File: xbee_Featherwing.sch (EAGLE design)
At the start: 17 parts

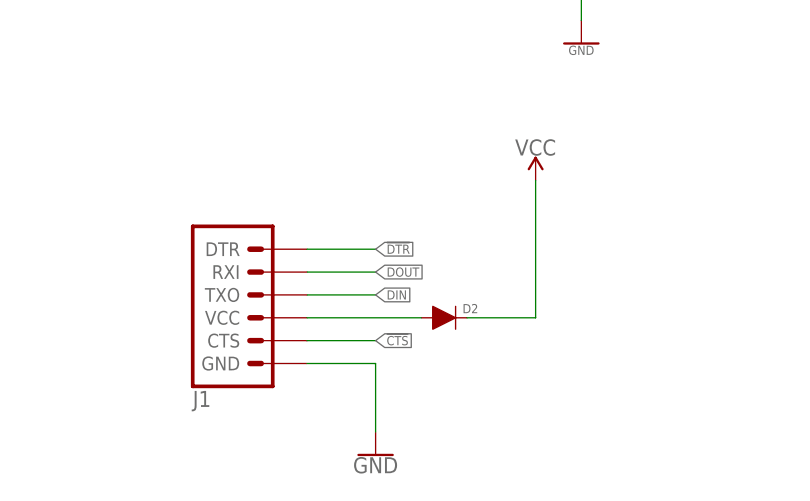
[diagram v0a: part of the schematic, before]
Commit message: Changing footprint
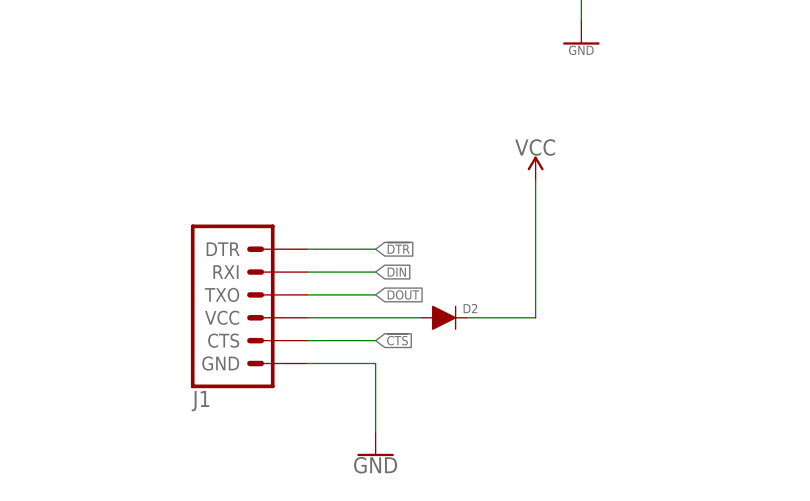
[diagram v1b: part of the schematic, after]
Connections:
- net DIN: now also J1.RXI; no longer J1.TXO
- net DOUT: now also J1.TXO; no longer J1.RXI
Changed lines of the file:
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@@
 <?xml version="1.0" encoding="utf-8"?>
 <!DOCTYPE eagle SYSTEM "eagle.dtd">
-<eagle version="9.5.0">
+<eagle version="9.4.1">
 <drawing>
 <settings>
@@
 </segment>
 <segment>
+<pinref part="MS1" gate="G$1" pin="GPIORX"/>
+<wire x1="55.88" y1="93.98" x2="50.8" y2="93.98" width="0.1524" layer="91"/>
+<label x="50.8" y="93.98" size="1.016" layer="95" font="vector" ratio="20" rot="R180" xref="yes"/>
+</segment>
+<segment>
+<pinref part="J1" gate="G$1" pin="TXO"/>
+<wire x1="185.42" y1="60.96" x2="193.04" y2="60.96" width="0.1524" layer="91"/>
+<label x="193.04" y="60.96" size="1.016" layer="95" font="vector" ratio="20" xref="yes"/>
+</segment>
+</net>
+<net name="DIN" class="0">
+<segment>
+<pinref part="JP1" gate="G$1" pin="DIN"/>
+<wire x1="149.86" y1="114.3" x2="142.24" y2="114.3" width="0.1524" layer="91"/>
+<label x="142.24" y="114.3" size="1.016" layer="95" font="vector" ratio="20" rot="R180" xref="yes"/>
+</segment>
+<segment>
+<pinref part="MS1" gate="G$1" pin="GPIOTX"/>
+<wire x1="55.88" y1="91.44" x2="50.8" y2="91.44" width="0.1524" layer="91"/>
+<label x="50.8" y="91.44" size="1.016" layer="95" font="vector" ratio="20" rot="R180" xref="yes"/>
+</segment>
+<segment>
 <pinref part="J1" gate="G$1" pin="RXI"/>
 <wire x1="185.42" y1="63.5" x2="193.04" y2="63.5" width="0.1524" layer="91"/>
 <label x="193.04" y="63.5" size="1.016" layer="95" font="vector" ratio="20" xref="yes"/>
 </segment>
-<segment>
-<pinref part="MS1" gate="G$1" pin="GPIORX"/>
-<wire x1="55.88" y1="93.98" x2="50.8" y2="93.98" width="0.1524" layer="91"/>
-<label x="50.8" y="93.98" size="1.016" layer="95" font="vector" ratio="20" rot="R180" xref="yes"/>
-</segment>
-</net>
-<net name="DIN" class="0">
-<segment>
-<pinref part="JP1" gate="G$1" pin="DIN"/>
-<wire x1="149.86" y1="114.3" x2="142.24" y2="114.3" width="0.1524" layer="91"/>
-<label x="142.24" y="114.3" size="1.016" layer="95" font="vector" ratio="20" rot="R180" xref="yes"/>
-</segment>
-<segment>
-<pinref part="J1" gate="G$1" pin="TXO"/>
-<wire x1="185.42" y1="60.96" x2="193.04" y2="60.96" width="0.1524" layer="91"/>
-<label x="193.04" y="60.96" size="1.016" layer="95" font="vector" ratio="20" xref="yes"/>
-</segment>
-<segment>
-<pinref part="MS1" gate="G$1" pin="GPIOTX"/>
-<wire x1="55.88" y1="91.44" x2="50.8" y2="91.44" width="0.1524" layer="91"/>
-<label x="50.8" y="91.44" size="1.016" layer="95" font="vector" ratio="20" rot="R180" xref="yes"/>
-</segment>
-</net>
+</net>
